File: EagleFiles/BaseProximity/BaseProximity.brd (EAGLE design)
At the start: 80 x 60 mm, 26 parts, among them Q1 2N3904, Q3 2N3904

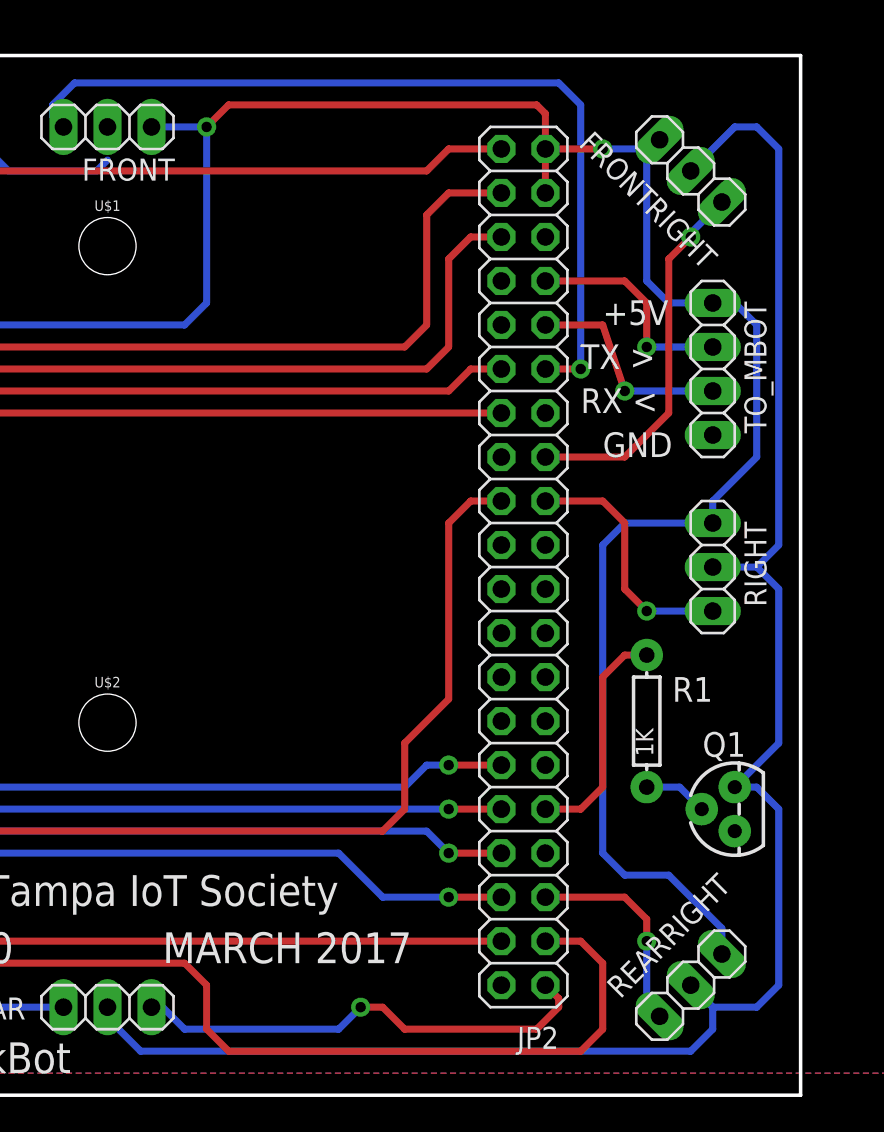
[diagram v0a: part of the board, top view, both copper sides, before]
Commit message: added additional instructions for building sensor board
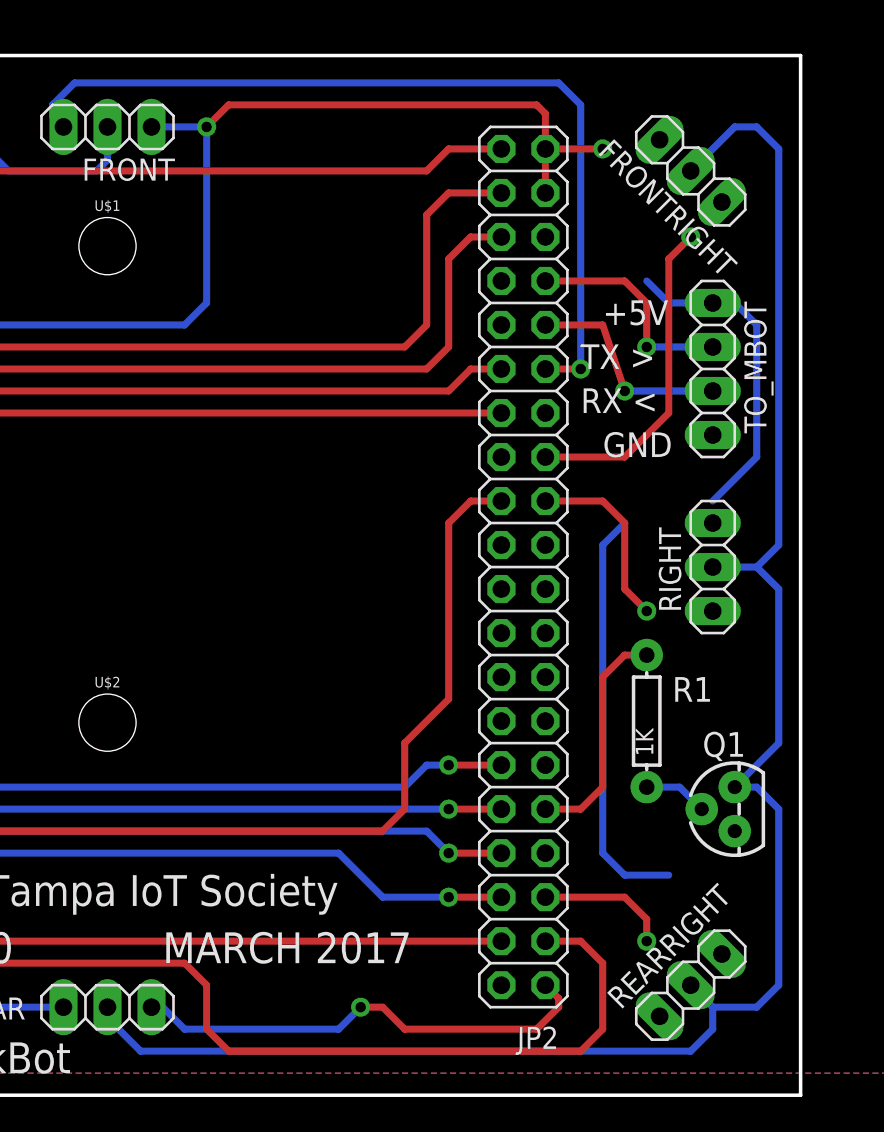
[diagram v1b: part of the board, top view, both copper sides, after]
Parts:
- turned FRONTRIGHT to 135 degrees
- turned REARRIGHT to 45 degrees
- turned RIGHT to 90 degrees
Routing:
- net +5V: track 260.0 -> 236.9 mm
- net GPIO16: track 12.6 -> 7.86 mm
- net GPIO24: track 14.5 -> 10.7 mm
- net GPIO23: track 21.6 -> 19.1 mm
- net IR_GND: track 111.1 -> 113.0 mm
- net IR_GND2: track 107.4 -> 105.6 mm
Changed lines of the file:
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@@
 <?xml version="1.0" encoding="utf-8"?>
 <!DOCTYPE eagle SYSTEM "eagle.dtd">
-<eagle version="8.0.2">
+<eagle version="7.7.0">
 <drawing>
 <settings>
@@
 </element>
 <element name="FRONT" library="pinhead" package="1X03" value="" x="40" y="55.88" rot="R180"/>
-<element name="FRONTRIGHT" library="pinhead" package="1X03" value="" x="73.66" y="53.34" smashed="yes" rot="R315">
-<attribute name="NAME" x="67.125196875" y="54.8411125" size="1.27" layer="25" ratio="10" rot="R315"/>
-<attribute name="VALUE" x="68.72085625" y="53.7890125" size="1.27" layer="27" rot="R315"/>
+<element name="FRONTRIGHT" library="pinhead" package="1X03" value="" x="73.66" y="53.34" smashed="yes" rot="R135">
+<attribute name="NAME" x="76.384803125" y="48.0288875" size="1.27" layer="25" ratio="10" rot="R135"/>
+<attribute name="VALUE" x="78.59914375" y="52.8909875" size="1.27" layer="27" rot="R135"/>
 </element>
 <element name="LEFT" library="pinhead" package="1X03" value="" x="3.81" y="29.21" smashed="yes" rot="R270">
@@
 <attribute name="VALUE" x="0.635" y="33.02" size="1.27" layer="27" rot="R270"/>
 </element>
-<element name="REARRIGHT" library="pinhead" package="1X03" value="" x="73.66" y="6.35" smashed="yes" rot="R225">
-<attribute name="NAME" x="75.1611125" y="12.8848" size="1.27" layer="25" ratio="10" rot="R225"/>
-<attribute name="VALUE" x="74.1090125" y="11.289140625" size="1.27" layer="27" rot="R225"/>
+<element name="REARRIGHT" library="pinhead" package="1X03" value="" x="73.66" y="6.35" smashed="yes" rot="R45">
+<attribute name="NAME" x="69.6188875" y="4.8952" size="1.27" layer="25" ratio="10" rot="R45"/>
+<attribute name="VALUE" x="73.2109875" y="1.410859375" size="1.27" layer="27" rot="R45"/>
 </element>
 <element name="REARLEFT" library="pinhead" package="1X03" value="" x="6.35" y="6.35" smashed="yes" rot="R315">
@@
 <attribute name="VALUE" x="36.19" y="1.905" size="1.27" layer="27"/>
 </element>
-<element name="RIGHT" library="pinhead" package="1X03" value="" x="74.93" y="30.48" smashed="yes" rot="R270">
-<attribute name="NAME" x="76.7588" y="33.0962" size="1.27" layer="25" ratio="10" rot="R270"/>
-<attribute name="VALUE" x="71.755" y="34.29" size="1.27" layer="27" rot="R270"/>
+<element name="RIGHT" library="pinhead" package="1X03" value="" x="74.93" y="30.48" smashed="yes" rot="R90">
+<attribute name="NAME" x="73.1012" y="27.8638" size="1.27" layer="25" ratio="10" rot="R90"/>
+<attribute name="VALUE" x="78.105" y="26.67" size="1.27" layer="27" rot="R90"/>
 </element>
 <element name="I2C_2" library="pinhead" package="1X04" value="" x="11.43" y="38.1" smashed="yes" rot="R180">
@@
 <contactref element="LEFT" pad="1"/>
 <wire x1="71.12" y1="54.61" x2="71.337896875" y2="54.61" width="0.4064" layer="16"/>
-<wire x1="71.337896875" y1="54.61" x2="71.863946875" y2="55.13605" width="0.4064" layer="16"/>
 <wire x1="74.93" y1="45.72" x2="72.39" y2="45.72" width="0.4064" layer="16"/>
 <wire x1="72.39" y1="45.72" x2="71.12" y2="46.99" width="0.4064" layer="16"/>
-<wire x1="71.12" y1="46.99" x2="71.12" y2="54.61" width="0.4064" layer="16"/>
 <wire x1="44.45" y1="44.45" x2="24.13" y2="44.45" width="0.4064" layer="16"/>
 <wire x1="24.13" y1="44.45" x2="22.86" y2="43.18" width="0.4064" layer="16"/>
@@
 <wire x1="65.27" y1="54.61" x2="68.58" y2="54.61" width="0.4064" layer="1"/>
 <via x="68.58" y="54.61" extent="1-16" drill="0.6" shape="octagon"/>
-<wire x1="68.58" y1="54.61" x2="71.12" y2="54.61" width="0.4064" layer="16"/>
 <wire x1="3.81" y1="45.72" x2="3.81" y2="31.75" width="0.4064" layer="16"/>
 <wire x1="65.27" y1="54.61" x2="65.27" y2="56.65" width="0.4064" layer="1"/>
@@
 <contactref element="RIGHT" pad="1"/>
 <contactref element="REARRIGHT" pad="1"/>
-<wire x1="75.45605" y1="8.14605" x2="75.45605" y2="9.63395" width="0.4064" layer="16"/>
-<wire x1="75.45605" y1="9.63395" x2="72.39" y2="12.7" width="0.4064" layer="16"/>
 <contactref element="REAR" pad="1"/>
 <contactref element="REARLEFT" pad="1"/>
@@
 <wire x1="68.58" y1="13.97" x2="69.85" y2="12.7" width="0.4064" layer="16"/>
 <wire x1="69.85" y1="12.7" x2="72.39" y2="12.7" width="0.4064" layer="16"/>
-<wire x1="74.93" y1="33.02" x2="69.85" y2="33.02" width="0.4064" layer="16"/>
 <wire x1="77.47" y1="44.45" x2="77.47" y2="36.83" width="0.4064" layer="16"/>
 <wire x1="77.47" y1="44.45" x2="76.2" y2="45.72" width="0.4064" layer="16"/>
 <wire x1="76.2" y1="45.72" x2="74.93" y2="45.72" width="0.4064" layer="16"/>
 <wire x1="19.05" y1="34.29" x2="21.59" y2="34.29" width="0.4064" layer="16"/>
-<wire x1="74.93" y1="34.29" x2="74.93" y2="33.02" width="0.4064" layer="16"/>
 <wire x1="77.47" y1="36.83" x2="74.93" y2="34.29" width="0.4064" layer="16"/>
 <wire x1="45.72" y1="45.72" x2="45.72" y2="55.88" width="0.4064" layer="16"/>
+<wire x1="71.337896875" y1="54.61" x2="75.45605" y2="51.543946875" width="0" layer="19" extent="16-16"/>
+<wire x1="68.58" y1="54.61" x2="71.12" y2="54.61" width="0" layer="19" extent="16-16"/>
+<wire x1="74.93" y1="45.72" x2="75.45605" y2="51.543946875" width="0" layer="19" extent="1-1"/>
+<wire x1="69.85" y1="33.02" x2="74.93" y2="34.29" width="0" layer="19" extent="16-16"/>
+<wire x1="74.93" y1="27.94" x2="74.93" y2="34.29" width="0" layer="19" extent="16-16"/>
+<wire x1="71.863946875" y1="4.553946875" x2="72.39" y2="12.7" width="0" layer="19" extent="16-16"/>
 </signal>
 <signal name="N$9">
@@
 <wire x1="71.12" y1="10.16" x2="71.12" y2="8.89" width="0.4064" layer="1"/>
 <via x="71.12" y="8.89" extent="1-16" drill="0.6" shape="octagon"/>
-<wire x1="71.863946875" y1="4.553946875" x2="71.646053125" y2="4.553946875" width="0.4064" layer="16"/>
-<wire x1="71.12" y1="8.89" x2="71.12" y2="5.08" width="0.4064" layer="16"/>
 <wire x1="71.12" y1="5.08" x2="71.33789375" y2="5.08" width="0.4064" layer="16"/>
-<wire x1="71.33789375" y1="5.08" x2="71.863946875" y2="4.553946875" width="0.4064" layer="16"/>
+<wire x1="71.12" y1="8.89" x2="75.45605" y2="8.14605" width="0" layer="19" extent="1-1"/>
+<wire x1="71.12" y1="5.08" x2="71.12" y2="8.89" width="0" layer="19" extent="16-16"/>
 </signal>
 <signal name="TX-RSP">
@@
 <via x="73.66" y="49.53" extent="1-16" drill="0.6" shape="octagon"/>
 <wire x1="73.66" y1="49.53" x2="73.66" y2="49.747896875" width="0.4064" layer="16"/>
-<wire x1="73.66" y1="49.747896875" x2="75.45605" y2="51.543946875" width="0.4064" layer="16"/>
+<wire x1="73.66" y1="49.747896875" x2="71.863946875" y2="55.13605" width="0" layer="19" extent="16-16"/>
 </signal>
 <signal name="GPIO24">
@@
 <wire x1="69.85" y1="29.21" x2="71.12" y2="27.94" width="0.4064" layer="1"/>
 <via x="71.12" y="27.94" extent="1-16" drill="0.6" shape="octagon"/>
-<wire x1="71.12" y1="27.94" x2="74.93" y2="27.94" width="0.4064" layer="16"/>
+<wire x1="69.85" y1="33.02" x2="74.93" y2="33.02" width="0" layer="19" extent="1-1"/>
 </signal>
 <signal name="GPIO25">
@@
 <wire x1="7.62" y1="10.16" x2="8.89" y2="11.43" width="0.4064" layer="16"/>
 <wire x1="8.89" y1="11.43" x2="10.16" y2="11.43" width="0.4064" layer="16"/>
-<wire x1="40" y1="53.97" x2="40" y2="55.88" width="0" layer="19" extent="16-16"/>
+<wire x1="40" y1="53.97" x2="40" y2="55.88" width="0.4064" layer="16"/>
 </signal>
 <signal name="N$1">
@@
 <wire x1="73.66" y1="2.54" x2="74.93" y2="3.81" width="0.4064" layer="16"/>
 <wire x1="74.93" y1="5.08" x2="74.93" y2="3.81" width="0.4064" layer="16"/>
-<wire x1="74.93" y1="5.08" x2="73.66" y2="6.35" width="0.4064" layer="16"/>
 <wire x1="73.66" y1="6.35" x2="74.93" y2="5.08" width="0.4064" layer="16"/>
 <wire x1="77.47" y1="17.78" x2="76.2" y2="17.78" width="0.4064" layer="16"/>

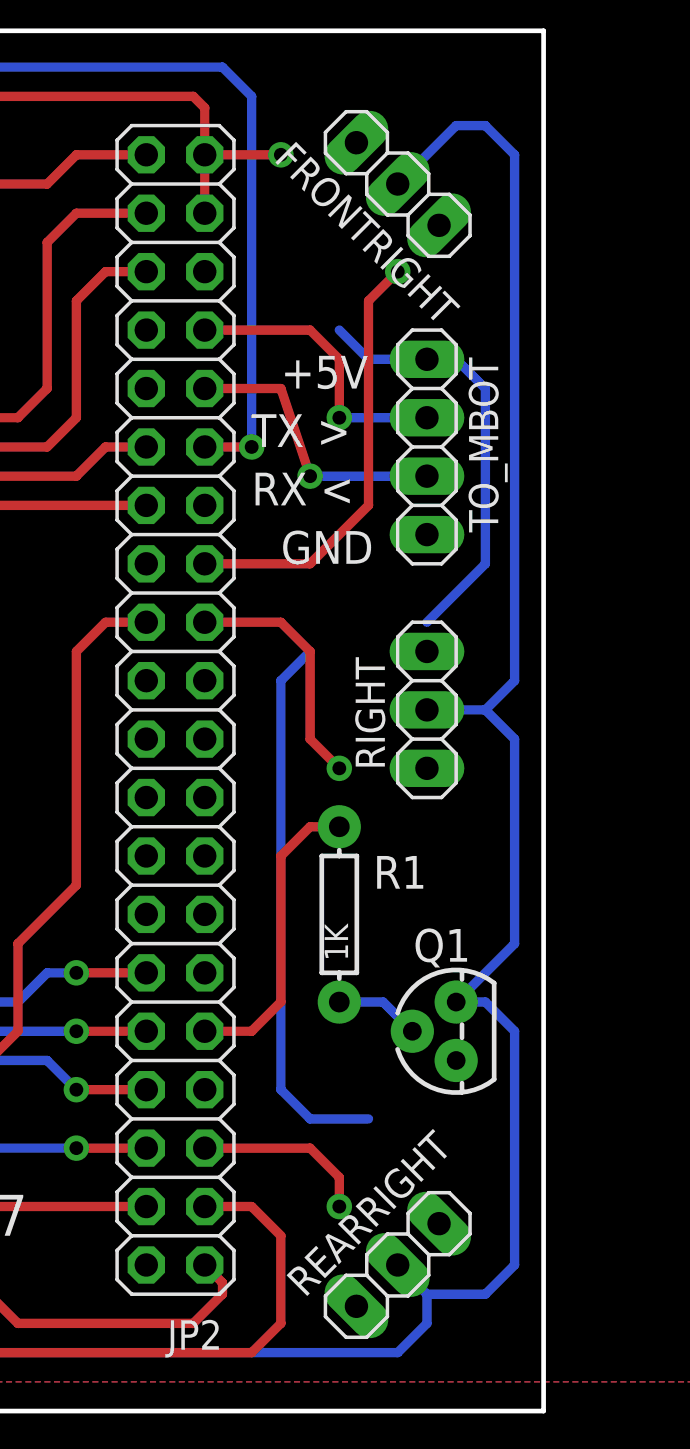
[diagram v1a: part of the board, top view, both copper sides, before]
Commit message: update instructions for board
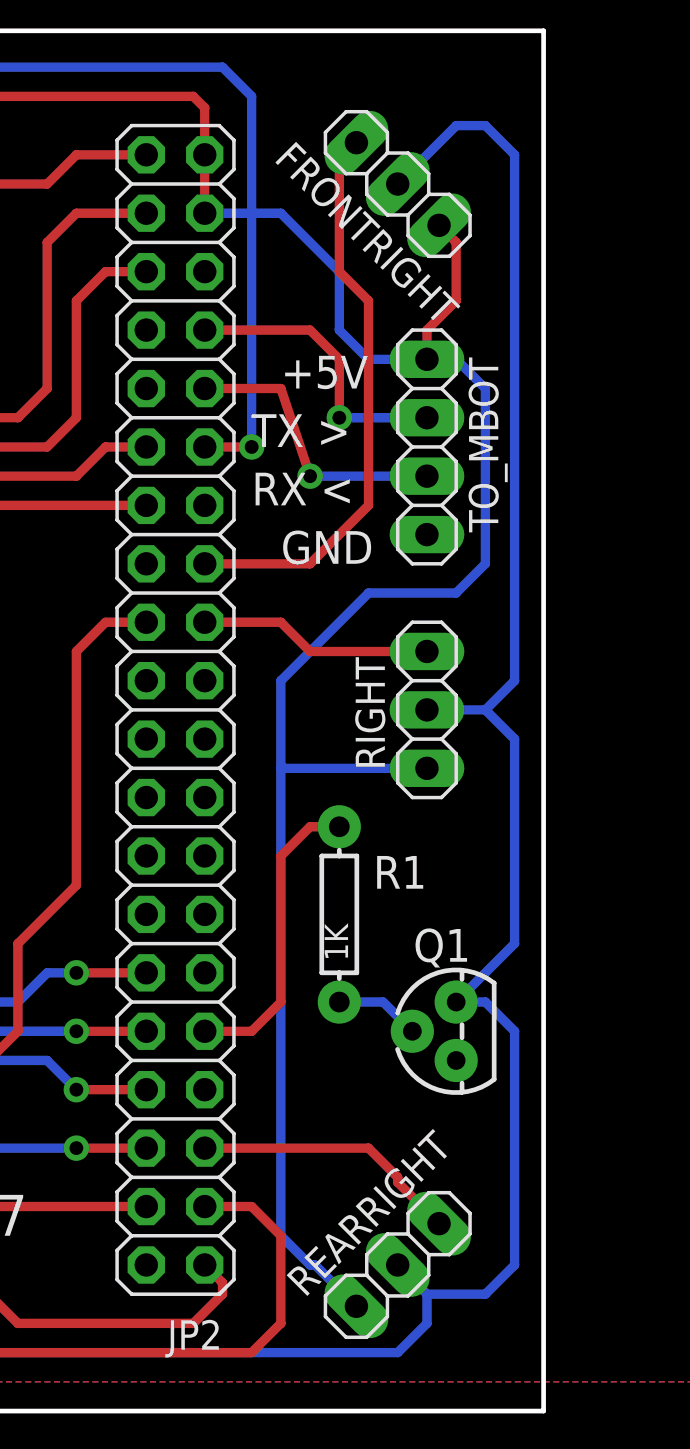
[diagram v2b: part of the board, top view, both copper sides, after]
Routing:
- net +5V: track 236.9 -> 268.0 mm, vias 2 -> 1
- net GPIO23: track 19.1 -> 24.8 mm, vias 1 -> 0
- net GPIO16: track 7.86 -> 11.7 mm, vias 1 -> 0
- net GPIO24: track 10.7 -> 10.2 mm, vias 1 -> 0
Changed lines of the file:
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@@
 <?xml version="1.0" encoding="utf-8"?>
 <!DOCTYPE eagle SYSTEM "eagle.dtd">
-<eagle version="7.7.0">
+<eagle version="8.0.2">
 <drawing>
 <settings>
@@
 <contactref element="FRONTRIGHT" pad="1"/>
 <contactref element="LEFT" pad="1"/>
-<wire x1="71.12" y1="54.61" x2="71.337896875" y2="54.61" width="0.4064" layer="16"/>
 <wire x1="74.93" y1="45.72" x2="72.39" y2="45.72" width="0.4064" layer="16"/>
 <wire x1="72.39" y1="45.72" x2="71.12" y2="46.99" width="0.4064" layer="16"/>
@@
 <wire x1="19.05" y1="22.86" x2="19.05" y2="27.94" width="0.4064" layer="16"/>
 <wire x1="65.27" y1="52.07" x2="65.27" y2="54.61" width="0.4064" layer="1"/>
-<wire x1="65.27" y1="54.61" x2="68.58" y2="54.61" width="0.4064" layer="1"/>
-<via x="68.58" y="54.61" extent="1-16" drill="0.6" shape="octagon"/>
 <wire x1="3.81" y1="45.72" x2="3.81" y2="31.75" width="0.4064" layer="16"/>
 <wire x1="65.27" y1="54.61" x2="65.27" y2="56.65" width="0.4064" layer="1"/>
@@
 <wire x1="3.81" y1="31.75" x2="10.16" y2="31.75" width="0.4064" layer="16"/>
 <wire x1="19.05" y1="27.94" x2="19.05" y2="34.29" width="0.4064" layer="16"/>
-<wire x1="69.85" y1="33.02" x2="68.58" y2="31.75" width="0.4064" layer="16"/>
-<wire x1="68.58" y1="31.75" x2="68.58" y2="13.97" width="0.4064" layer="16"/>
-<wire x1="68.58" y1="13.97" x2="69.85" y2="12.7" width="0.4064" layer="16"/>
-<wire x1="69.85" y1="12.7" x2="72.39" y2="12.7" width="0.4064" layer="16"/>
-<wire x1="77.47" y1="44.45" x2="77.47" y2="36.83" width="0.4064" layer="16"/>
+<wire x1="77.47" y1="36.83" x2="77.47" y2="44.45" width="0.4064" layer="16"/>
 <wire x1="77.47" y1="44.45" x2="76.2" y2="45.72" width="0.4064" layer="16"/>
 <wire x1="76.2" y1="45.72" x2="74.93" y2="45.72" width="0.4064" layer="16"/>
 <wire x1="19.05" y1="34.29" x2="21.59" y2="34.29" width="0.4064" layer="16"/>
-<wire x1="77.47" y1="36.83" x2="74.93" y2="34.29" width="0.4064" layer="16"/>
 <wire x1="45.72" y1="45.72" x2="45.72" y2="55.88" width="0.4064" layer="16"/>
-<wire x1="71.337896875" y1="54.61" x2="75.45605" y2="51.543946875" width="0" layer="19" extent="16-16"/>
-<wire x1="68.58" y1="54.61" x2="71.12" y2="54.61" width="0" layer="19" extent="16-16"/>
-<wire x1="74.93" y1="45.72" x2="75.45605" y2="51.543946875" width="0" layer="19" extent="1-1"/>
-<wire x1="69.85" y1="33.02" x2="74.93" y2="34.29" width="0" layer="19" extent="16-16"/>
-<wire x1="74.93" y1="27.94" x2="74.93" y2="34.29" width="0" layer="19" extent="16-16"/>
-<wire x1="71.863946875" y1="4.553946875" x2="72.39" y2="12.7" width="0" layer="19" extent="16-16"/>
+<wire x1="68.58" y1="7.62" x2="69.85" y2="6.35" width="0.4064" layer="16"/>
+<wire x1="69.85" y1="6.35" x2="70.06789375" y2="6.35" width="0.4064" layer="16"/>
+<wire x1="70.06789375" y1="6.35" x2="71.863946875" y2="4.553946875" width="0.4064" layer="16"/>
+<wire x1="68.58" y1="27.94" x2="68.58" y2="7.62" width="0.4064" layer="16"/>
+<wire x1="68.58" y1="27.94" x2="68.58" y2="31.75" width="0.4064" layer="16"/>
+<wire x1="72.39" y1="35.56" x2="76.2" y2="35.56" width="0.4064" layer="16"/>
+<wire x1="76.2" y1="35.56" x2="77.47" y2="36.83" width="0.4064" layer="16"/>
+<wire x1="68.58" y1="31.75" x2="72.39" y2="35.56" width="0.4064" layer="16"/>
+<wire x1="74.93" y1="27.94" x2="68.58" y2="27.94" width="0.4064" layer="16"/>
+<wire x1="74.93" y1="45.72" x2="74.93" y2="46.99" width="0.4064" layer="1"/>
+<wire x1="74.93" y1="46.99" x2="76.2" y2="48.26" width="0.4064" layer="1"/>
+<wire x1="76.2" y1="48.26" x2="76.2" y2="50.799996875" width="0.4064" layer="1"/>
+<wire x1="76.2" y1="50.799996875" x2="75.45605" y2="51.543946875" width="0.4064" layer="1"/>
+<wire x1="71.12" y1="46.99" x2="71.12" y2="49.53" width="0.4064" layer="16"/>
+<wire x1="71.12" y1="49.53" x2="68.58" y2="52.07" width="0.4064" layer="16"/>
+<wire x1="68.58" y1="52.07" x2="65.27" y2="52.07" width="0.4064" layer="16"/>
 </signal>
 <signal name="N$9">
@@
 <contactref element="JP2" pad="36"/>
 <contactref element="REARRIGHT" pad="3"/>
-<wire x1="65.27" y1="11.43" x2="69.85" y2="11.43" width="0.4064" layer="1"/>
-<wire x1="69.85" y1="11.43" x2="71.12" y2="10.16" width="0.4064" layer="1"/>
-<wire x1="71.12" y1="10.16" x2="71.12" y2="8.89" width="0.4064" layer="1"/>
-<via x="71.12" y="8.89" extent="1-16" drill="0.6" shape="octagon"/>
-<wire x1="71.12" y1="5.08" x2="71.33789375" y2="5.08" width="0.4064" layer="16"/>
-<wire x1="71.12" y1="8.89" x2="75.45605" y2="8.14605" width="0" layer="19" extent="1-1"/>
-<wire x1="71.12" y1="5.08" x2="71.12" y2="8.89" width="0" layer="19" extent="16-16"/>
+<wire x1="72.39" y1="11.43" x2="73.66" y2="10.16" width="0.4064" layer="1"/>
+<wire x1="73.66" y1="10.16" x2="73.66" y2="9.9421" width="0.4064" layer="1"/>
+<wire x1="73.66" y1="9.9421" x2="75.45605" y2="8.14605" width="0.4064" layer="1"/>
+<wire x1="65.27" y1="11.43" x2="72.39" y2="11.43" width="0.4064" layer="1"/>
 </signal>
 <signal name="TX-RSP">
@@
 <wire x1="69.85" y1="36.83" x2="72.39" y2="39.37" width="0.4064" layer="1"/>
 <wire x1="72.39" y1="39.37" x2="72.39" y2="48.26" width="0.4064" layer="1"/>
-<wire x1="72.39" y1="48.26" x2="73.66" y2="49.53" width="0.4064" layer="1"/>
-<via x="73.66" y="49.53" extent="1-16" drill="0.6" shape="octagon"/>
-<wire x1="73.66" y1="49.53" x2="73.66" y2="49.747896875" width="0.4064" layer="16"/>
-<wire x1="73.66" y1="49.747896875" x2="71.863946875" y2="55.13605" width="0" layer="19" extent="16-16"/>
+<wire x1="72.39" y1="48.26" x2="71.12" y2="49.53" width="0.4064" layer="1"/>
+<wire x1="71.12" y1="54.392103125" x2="71.863946875" y2="55.13605" width="0.4064" layer="1"/>
+<wire x1="71.12" y1="49.53" x2="71.12" y2="54.392103125" width="0.4064" layer="1"/>
 </signal>
 <signal name="GPIO24">
@@
 <wire x1="65.27" y1="34.29" x2="68.58" y2="34.29" width="0.4064" layer="1"/>
 <wire x1="68.58" y1="34.29" x2="69.85" y2="33.02" width="0.4064" layer="1"/>
-<wire x1="69.85" y1="33.02" x2="69.85" y2="29.21" width="0.4064" layer="1"/>
-<wire x1="69.85" y1="29.21" x2="71.12" y2="27.94" width="0.4064" layer="1"/>
-<via x="71.12" y="27.94" extent="1-16" drill="0.6" shape="octagon"/>
-<wire x1="69.85" y1="33.02" x2="74.93" y2="33.02" width="0" layer="19" extent="1-1"/>
+<wire x1="69.85" y1="33.02" x2="74.93" y2="33.02" width="0.4064" layer="1"/>
 </signal>
 <signal name="GPIO25">
